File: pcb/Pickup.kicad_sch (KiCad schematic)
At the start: 35 parts, among them IC1 MAX9924UAUB+, K1 AQY212EHAX, T1 SM-LP-5001E

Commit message: video call revision
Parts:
- JP1: footprint (none) -> Jumper:SolderJumper-2_P1.3mm_Open_RoundedPad1.0x1.5mm
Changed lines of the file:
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@@
 			)
 		)
-		(property "Footprint" ""
+		(property "Footprint" "Jumper:SolderJumper-2_P1.3mm_Open_RoundedPad1.0x1.5mm"
 			(at 93.98 55.88 0)
 			(effects

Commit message: added footprints
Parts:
- D1: footprint DIONM5336X265N -> SamacSys_Parts:DIONM5336X265N
- IC1: footprint SOP50P490X110-10N -> SamacSys_Parts:SOP50P490X110-10N
- K1: footprint AQY212EHAX -> SamacSys_Parts:AQY212EHAX
- T1: footprint SMLP5001E -> SamacSys_Parts:SMLP5001E
- TP1, TP2, TP3, TP4, TP5, TP6, TP7, TP8: footprint (none) -> Connector_PinHeader_1.00mm:PinHeader_1x01_P1.00mm_Vertical
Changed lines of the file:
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@@
 			)
 		)
-		(property "Footprint" ""
+		(property "Footprint" "Connector_PinHeader_1.00mm:PinHeader_1x01_P1.00mm_Vertical"
 			(at 127 24.13 0)
 			(effects
@@
 			)
 		)
-		(property "Footprint" ""
+		(property "Footprint" "Connector_PinHeader_1.00mm:PinHeader_1x01_P1.00mm_Vertical"
 			(at 44.45 120.65 0)
 			(effects
@@
 			)
 		)
-		(property "Footprint" ""
+		(property "Footprint" "Connector_PinHeader_1.00mm:PinHeader_1x01_P1.00mm_Vertical"
 			(at 215.9 41.91 0)
 			(effects
@@
 			)
 		)
-		(property "Footprint" ""
+		(property "Footprint" "Connector_PinHeader_1.00mm:PinHeader_1x01_P1.00mm_Vertical"
 			(at 129.54 120.65 0)
 			(effects
@@
 			)
 		)
-		(property "Footprint" "SMLP5001E"
+		(property "Footprint" "SamacSys_Parts:SMLP5001E"
 			(at 80.01 26.67 0)
 			(effects
@@
 			)
 		)
-		(property "Footprint" "SOP50P490X110-10N"
+		(property "Footprint" "SamacSys_Parts:SOP50P490X110-10N"
 			(at 102.87 133.35 0)
 			(effects
@@
 			)
 		)
-		(property "Footprint" "DIONM5336X265N"
+		(property "Footprint" "SamacSys_Parts:DIONM5336X265N"
 			(at 90.17 38.1 0)
 			(effects
@@
 			)
 		)
-		(property "Footprint" ""
+		(property "Footprint" "Connector_PinHeader_1.00mm:PinHeader_1x01_P1.00mm_Vertical"
 			(at 254 41.91 0)
 			(effects
@@
 			)
 		)
-		(property "Footprint" "AQY212EHAX"
+		(property "Footprint" "SamacSys_Parts:AQY212EHAX"
 			(at 237.49 43.18 0)
 			(effects
@@
 			)
 		)
-		(property "Footprint" ""
+		(property "Footprint" "Connector_PinHeader_1.00mm:PinHeader_1x01_P1.00mm_Vertical"
 			(at 165.1 157.48 0)
 			(effects
@@
 			)
 		)
-		(property "Footprint" ""
+		(property "Footprint" "Connector_PinHeader_1.00mm:PinHeader_1x01_P1.00mm_Vertical"
 			(at 128.27 57.15 0)
 			(effects
@@
 			)
 		)
-		(property "Footprint" ""
+		(property "Footprint" "Connector_PinHeader_1.00mm:PinHeader_1x01_P1.00mm_Vertical"
 			(at 44.45 133.35 0)
 			(effects

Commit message: added connector and simulation link
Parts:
- added JP16, JP17: SolderJumper_2_Open, Jumper:SolderJumper-2_P1.3mm_Open_RoundedPad1.0x1.5mm, symbol Jumper:SolderJumper_2_Open
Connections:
- net PICKUP_SIM_IN+: now also JP16.2 (B)
- net PICKUP_SIM_IN-: now also JP17.2 (B)
- net VR+: now also JP16.1 (A)
- net VR-: now also JP17.1 (A)

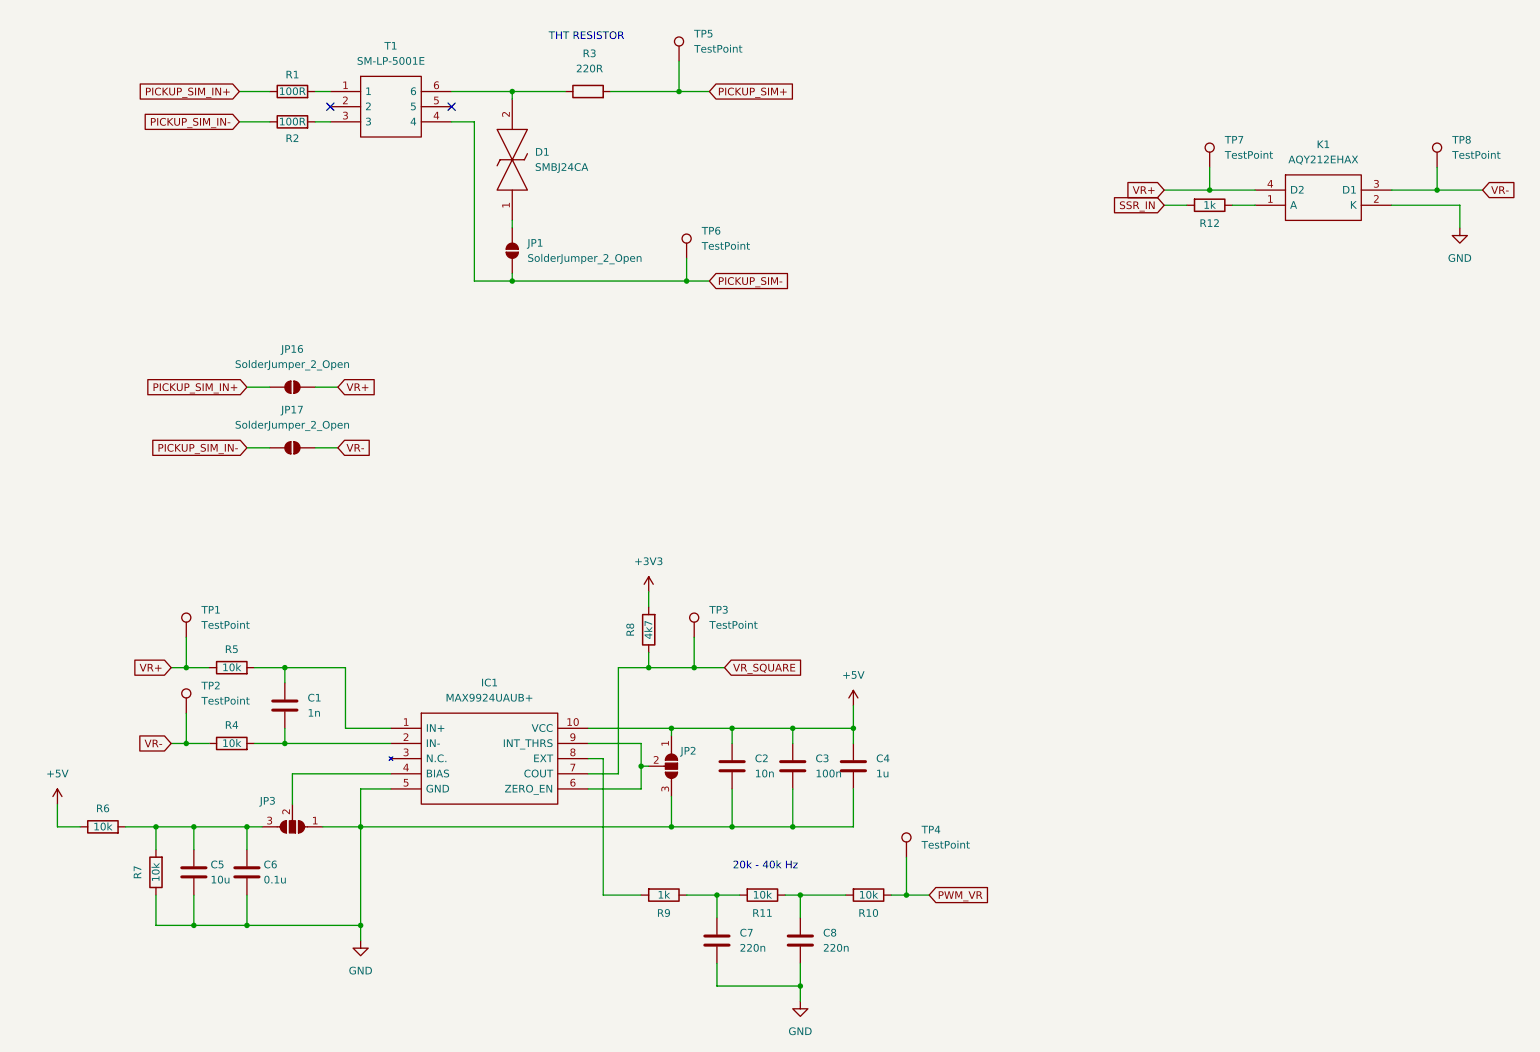
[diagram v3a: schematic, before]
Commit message: enhanced pickup simulation
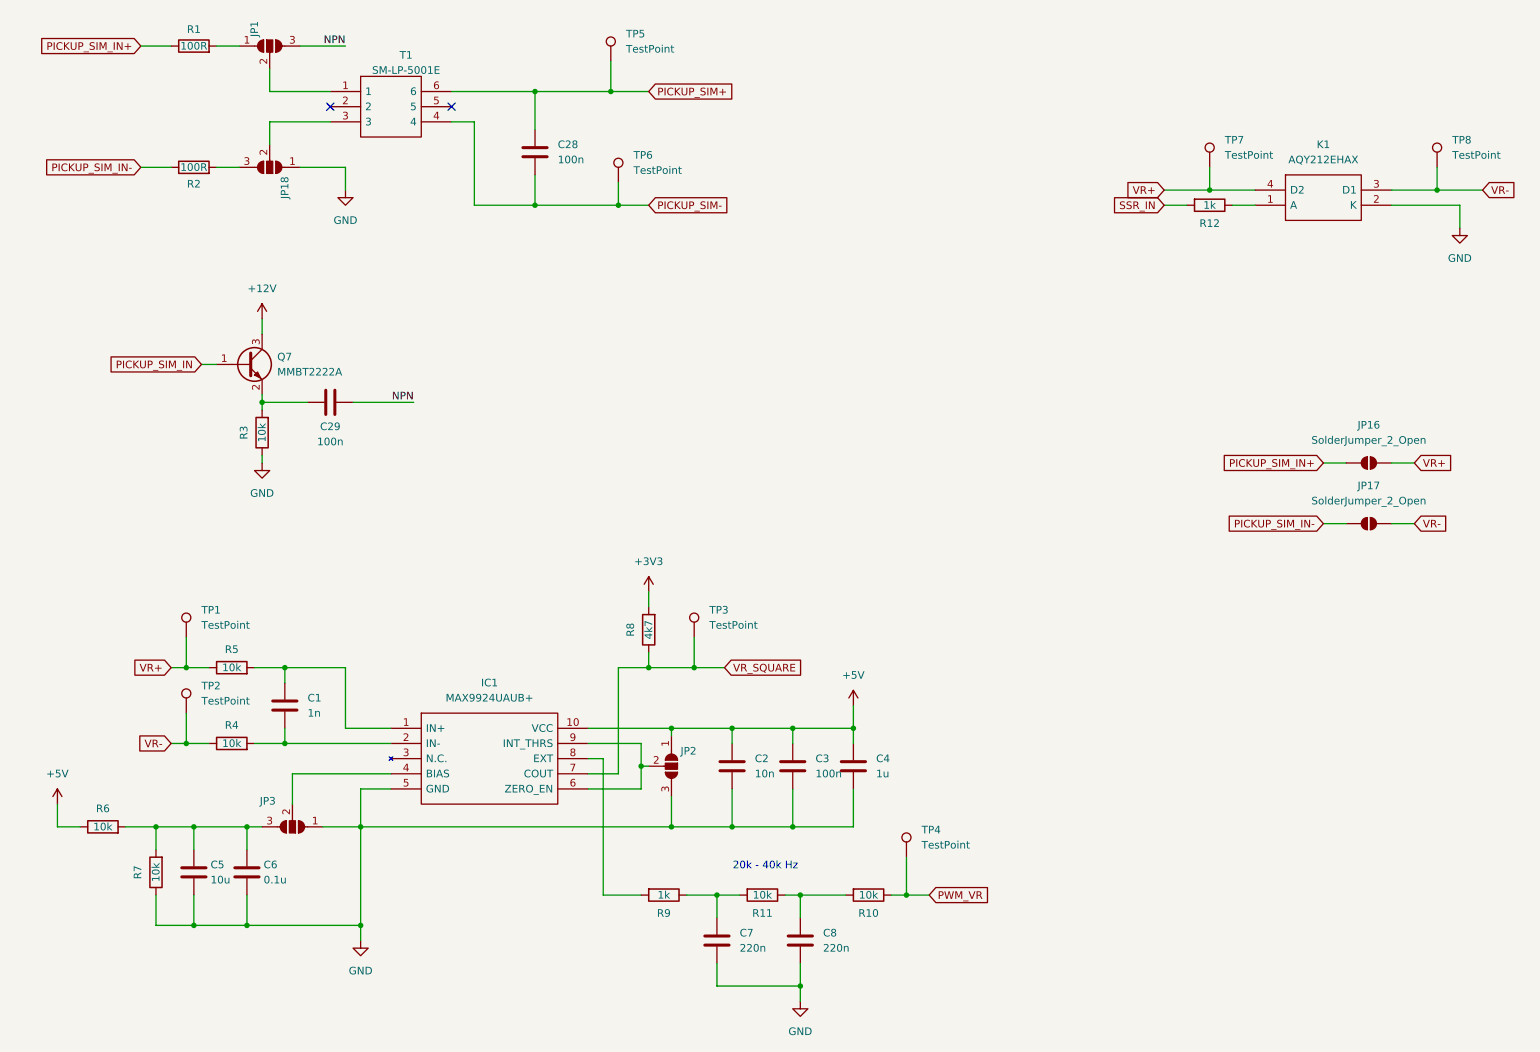
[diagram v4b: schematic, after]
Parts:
- removed D1: SMBJ24CA, SamacSys_Parts:DIONM5336X265N, symbol SamacSys_Parts:SMBJ24CA
- removed JP1: SolderJumper_2_Open, Jumper:SolderJumper-2_P1.3mm_Open_RoundedPad1.0x1.5mm, symbol Jumper:SolderJumper_2_Open
- added C28, C29: 100n, Capacitor_THT:C_Disc_D4.3mm_W1.9mm_P5.00mm, symbol Device:C
- added JP1, JP18: SolderJumper_3_Open, Jumper:SolderJumper-3_P1.3mm_Open_RoundedPad1.0x1.5mm, symbol Jumper:SolderJumper_3_Open
- added Q7: MMBT2222A, Package_TO_SOT_SMD:SOT-23, symbol Transistor_BJT:MMBT2222A
- R3: value 220R -> 10k
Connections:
- net GND: now also R3.1, JP18.1 (A)
- net PICKUP_SIM+: now also T1.6, C28.1; no longer R3.2
- net PICKUP_SIM-: now also C28.2
- net at T1.1: now also JP1.2 (C); no longer R1.2
- net at T1.3: now also JP18.2 (C); no longer R2.2
- new net: JP1.1 (A), R1.2
- new net: JP18.3 (B), R2.2
- new net: C29.1, Q7.2 (E), R3.2
- new net +12V: Q7.3 (C)
- new net NPN: C29.2, JP1.3 (B)
- new net PICKUP_SIM_IN: Q7.1 (B)
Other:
- note removed: "THT RESISTOR"
- moved on the sheet: JP16, JP17, R1, R2, TP5, TP6

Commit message: changed capacitors and resistors footprints from 0201 to 0603
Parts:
- C1, C2, C3, C4, C5, C6, C7, C8: footprint Capacitor_SMD:C_0201_0603Metric -> Capacitor_SMD:C_0603_1608Metric
- R10, R11, R12, R6, R7, R8, R9: footprint Resistor_SMD:R_0201_0603Metric -> Resistor_SMD:R_0603_1608Metric
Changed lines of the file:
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@@
 			)
 		)
-		(property "Footprint" "Resistor_SMD:R_0201_0603Metric"
+		(property "Footprint" "Resistor_SMD:R_0603_1608Metric"
 			(at 25.4 154.178 90)
 			(effects
@@
 			)
 		)
-		(property "Footprint" "Capacitor_SMD:C_0201_0603Metric"
+		(property "Footprint" "Capacitor_SMD:C_0603_1608Metric"
 			(at 56.8452 135.89 0)
 			(effects
@@
 			)
 		)
-		(property "Footprint" "Resistor_SMD:R_0201_0603Metric"
+		(property "Footprint" "Resistor_SMD:R_0603_1608Metric"
 			(at 210.82 46.482 90)
 			(effects
@@
 			)
 		)
-		(property "Footprint" "Resistor_SMD:R_0201_0603Metric"
+		(property "Footprint" "Resistor_SMD:R_0603_1608Metric"
 			(at 119.38 162.052 90)
 			(effects
@@
 			)
 		)
-		(property "Footprint" "Resistor_SMD:R_0201_0603Metric"
+		(property "Footprint" "Resistor_SMD:R_0603_1608Metric"
 			(at 36.068 160.02 90)
 			(effects
@@
 			)
 		)
-		(property "Footprint" "Capacitor_SMD:C_0201_0603Metric"
+		(property "Footprint" "Capacitor_SMD:C_0603_1608Metric"
 			(at 152.0952 146.05 0)
 			(effects
@@
 			)
 		)
-		(property "Footprint" "Resistor_SMD:R_0201_0603Metric"
+		(property "Footprint" "Resistor_SMD:R_0603_1608Metric"
 			(at 118.618 119.38 90)
 			(effects
@@
 			)
 		)
-		(property "Footprint" "Capacitor_SMD:C_0201_0603Metric"
+		(property "Footprint" "Capacitor_SMD:C_0603_1608Metric"
 			(at 131.7752 146.05 0)
 			(effects
@@
 			)
 		)
-		(property "Footprint" "Capacitor_SMD:C_0201_0603Metric"
+		(property "Footprint" "Capacitor_SMD:C_0603_1608Metric"
 			(at 141.9352 146.05 0)
 			(effects
@@
 			)
 		)
-		(property "Footprint" "Capacitor_SMD:C_0201_0603Metric"
+		(property "Footprint" "Capacitor_SMD:C_0603_1608Metric"
 			(at 41.6052 163.83 0)
 			(effects
@@
 			)
 		)
-		(property "Footprint" "Resistor_SMD:R_0201_0603Metric"
+		(property "Footprint" "Resistor_SMD:R_0603_1608Metric"
 			(at 135.89 162.052 90)
 			(effects
@@
 			)
 		)
-		(property "Footprint" "Capacitor_SMD:C_0201_0603Metric"
+		(property "Footprint" "Capacitor_SMD:C_0603_1608Metric"
 			(at 50.4952 163.83 0)
 			(effects
@@
 			)
 		)
-		(property "Footprint" "Capacitor_SMD:C_0201_0603Metric"
+		(property "Footprint" "Capacitor_SMD:C_0603_1608Metric"
 			(at 143.2052 175.26 0)
 			(effects
@@
 			)
 		)
-		(property "Footprint" "Capacitor_SMD:C_0201_0603Metric"
+		(property "Footprint" "Capacitor_SMD:C_0603_1608Metric"
 			(at 129.2352 175.26 0)
 			(effects
@@
 			)
 		)
-		(property "Footprint" "Resistor_SMD:R_0201_0603Metric"
+		(property "Footprint" "Resistor_SMD:R_0603_1608Metric"
 			(at 153.67 162.052 90)
 			(effects

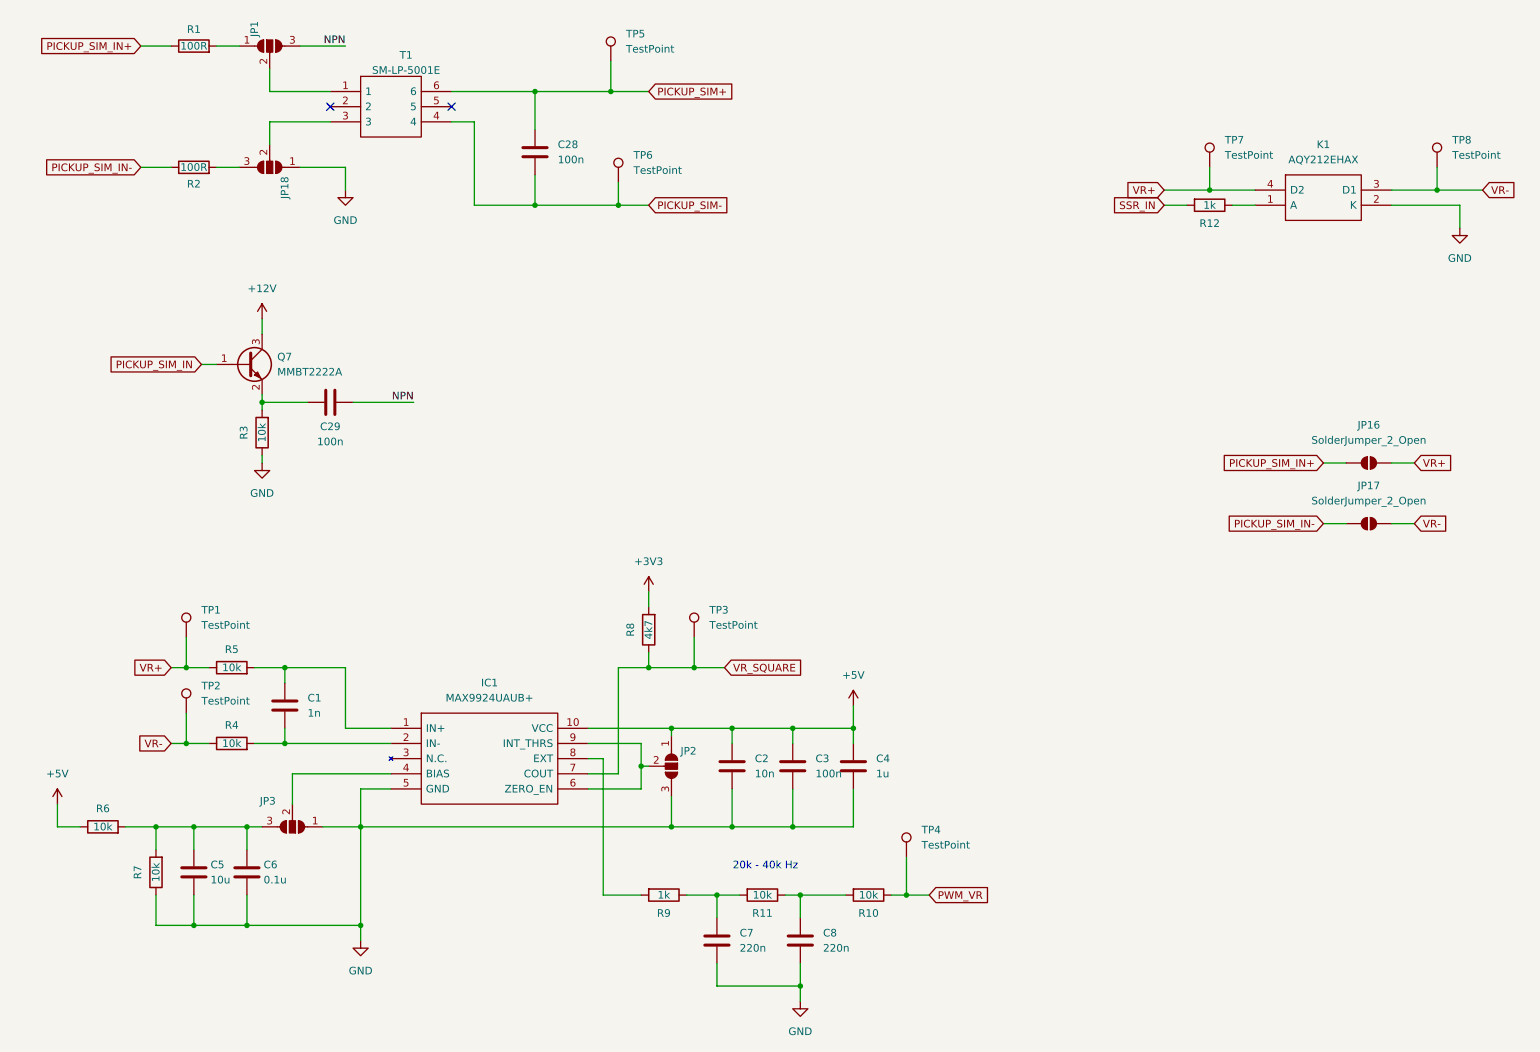
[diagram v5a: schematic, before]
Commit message: changed SCR drives to pnp drive and started schematic revision
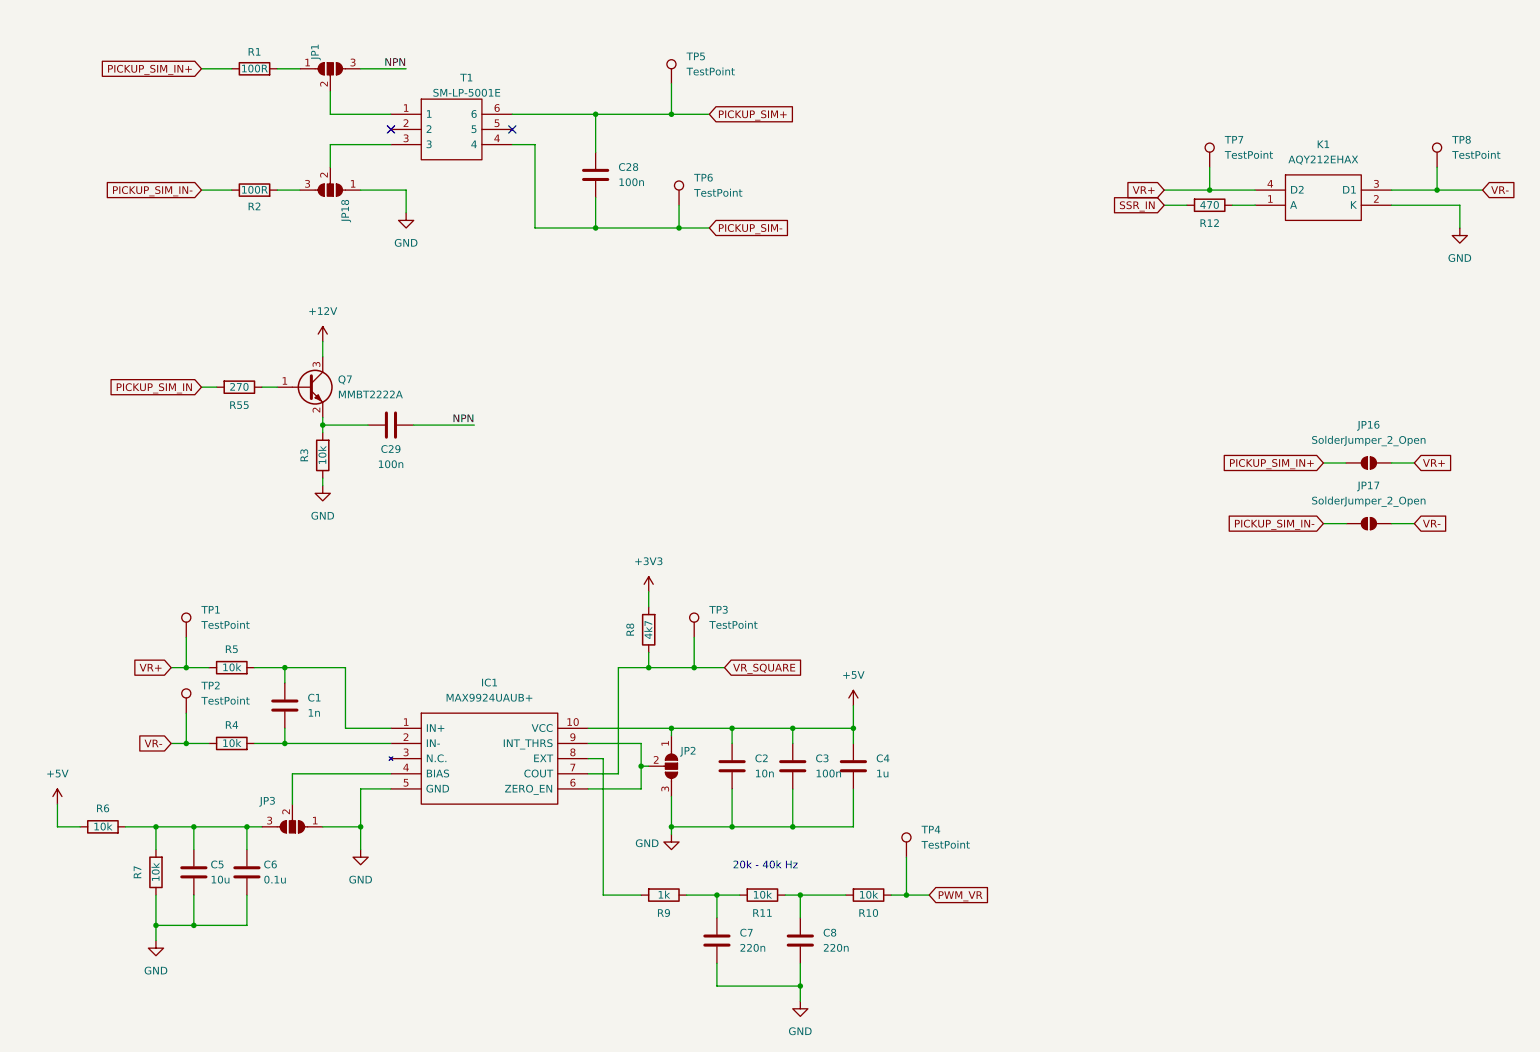
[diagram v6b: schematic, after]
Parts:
- added R55: 270, Resistor_SMD:R_0603_1608Metric, symbol Device:R
- R12: value 1k -> 470
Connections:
- net PICKUP_SIM_IN: now also R55.2; no longer Q7.1 (B)
- new net: Q7.1 (B), R55.1
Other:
- moved on the sheet: C28, C29, JP1, JP18, Q7, R1, R2, R3, T1, TP5, TP6
